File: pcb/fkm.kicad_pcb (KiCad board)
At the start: 2 copper layers, 50.3 x 33.5 mm, 12 parts, among them U2 18650, U3 AMS1117-3.3

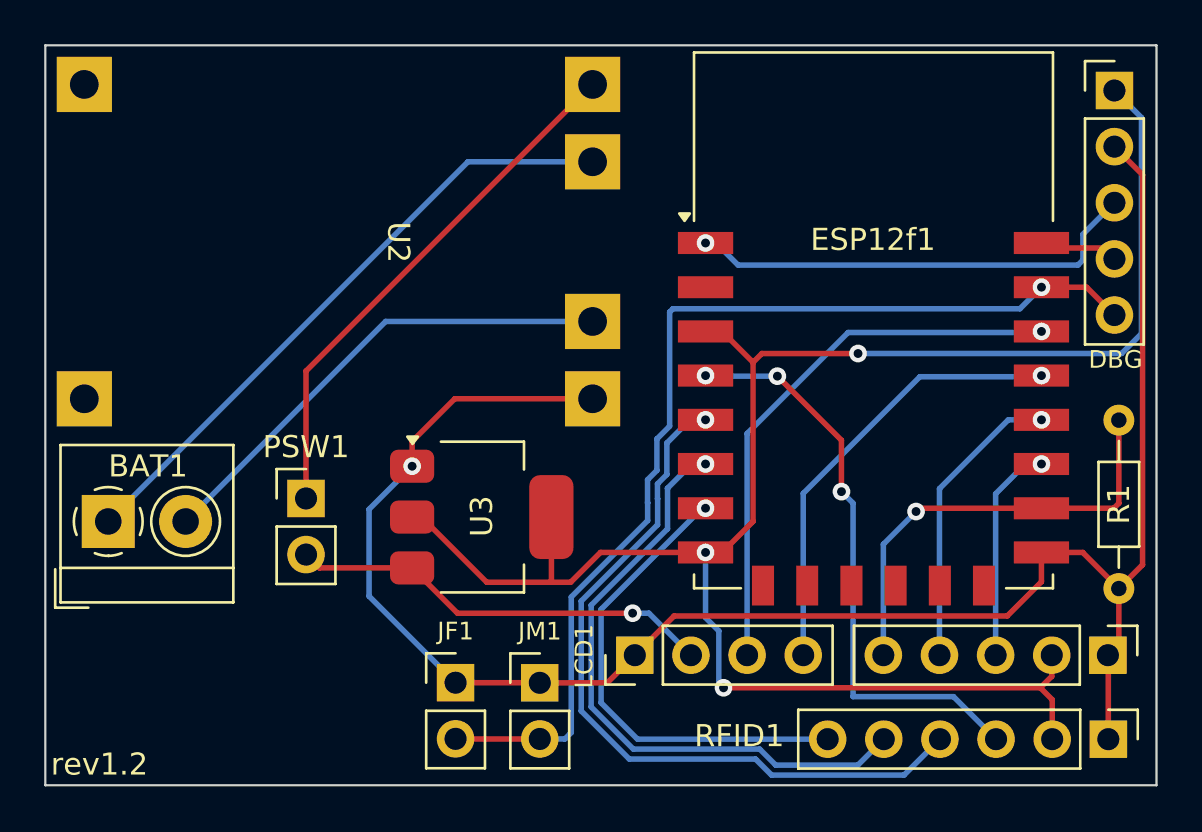
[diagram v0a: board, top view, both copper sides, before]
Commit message: wip(pcb): rev 2.0 pcb (esp32) - to re-do
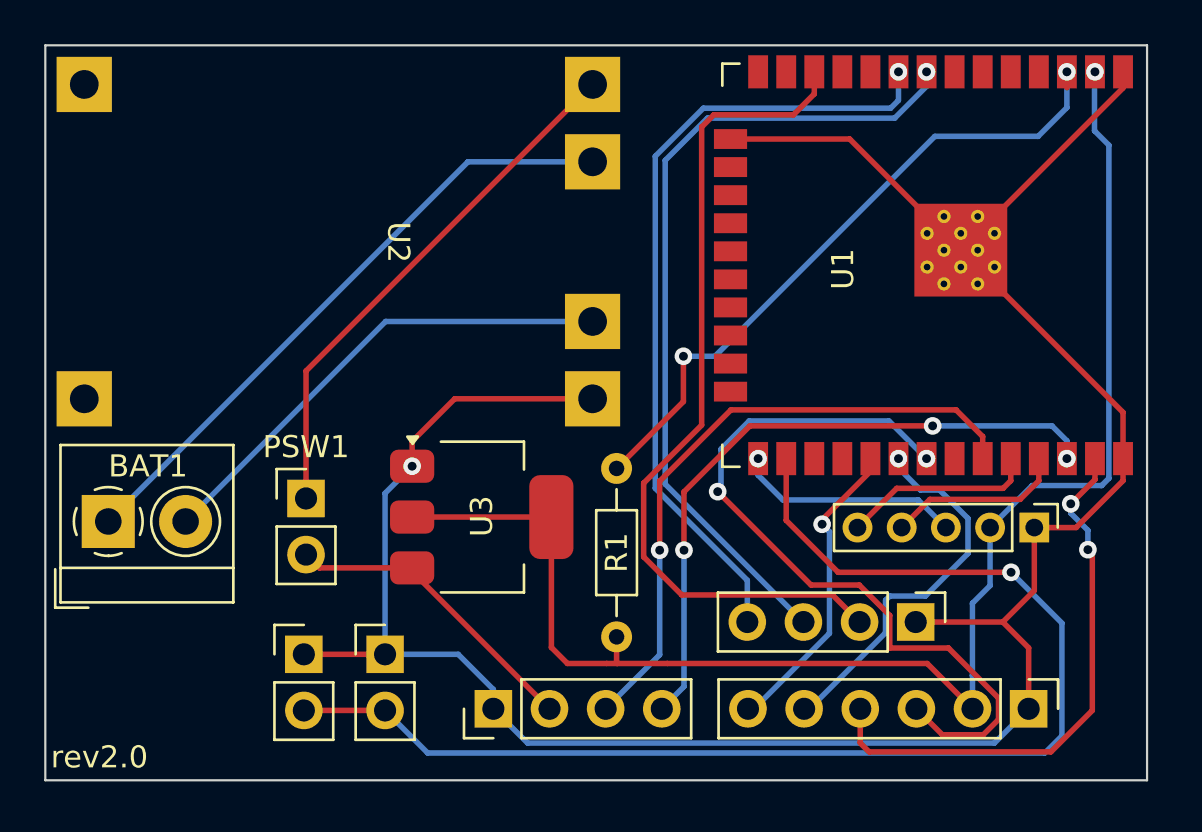
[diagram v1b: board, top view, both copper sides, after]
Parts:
- removed ESP12f1: ESP-12F/E, RF_Module:ESP-12E
- added U1: ESP32-WROOM-32, RF_Module:ESP32-WROOM-32, F.Cu at (107.2, 84.7)
- BTN1: value Conn_01x05 -> Conn_01x04; footprint Connector_PinHeader_2.54mm:PinHeader_1x05_P2.54mm_Vertical -> Connector_PinHeader_2.54mm:PinHeader_1x04_P2.54mm_Vertical
- DBG1: footprint Connector_PinHeader_2.54mm:PinHeader_1x05_P2.54mm_Vertical -> Connector_PinHeader_2.00mm:PinHeader_1x05_P2.00mm_Vertical
- moved R1 24.8 mm to (92.5, 101.5), turned to 90 degrees
- moved DBG1 20.1 mm to (111.4, 96.6), turned to -90 degrees
- moved BTN1 8.82 mm to (106.1, 100.9)
- moved JM1 7.12 mm to (82.0, 102.3)
- moved JF1 6.98 mm to (78.4, 102.3)
- moved LCD1 6.84 mm to (87.0, 104.8)
- moved RFID1 3.86 mm to (111.2, 104.8)
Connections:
- BTN1 pad 2: +3.3V -> Net-(BTN1-Pin_2)
- DBG1 pad 1: +3.3V -> GND
- DBG1 pad 2: GND -> +3.3V
- DBG1 pad 3: Net-(DBG1-Pin_3) -> BM
- DBG1 pad 4: Net-(DBG1-Pin_4) -> TX
- DBG1 pad 5: Net-(DBG1-Pin_5) -> RX
- JF1 pad 2: Net-(DBG1-Pin_5) -> JACK
- JM1 pad 2: Net-(DBG1-Pin_5) -> JACK
- LCD1 pad 3: Net-(ESP12f1-GPIO5) -> SDA
- LCD1 pad 4: Net-(ESP12f1-GPIO4) -> SCL
- R1 pad 1: Net-(BTN1-Pin_5) -> +3.3V
- R1 pad 2: GND -> Net-(U1-EN)
- RFID1 pad 3: Net-(ESP12f1-GPIO16) -> MISO
- RFID1 pad 4: Net-(ESP12f1-GPIO14) -> MOSI
- RFID1 pad 5: Net-(ESP12f1-GPIO12) -> SCK
- RFID1 pad 6: Net-(ESP12f1-GPIO13) -> CS
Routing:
- net JACK: track 0.00 -> 57.7 mm, vias 0 -> 1
- net Net-(DBG1-Pin_5): track 47.3 -> 0.00 mm, vias 1 -> 0
- net Net-(BTN1-Pin_2): track 0.00 -> 38.2 mm
- net MISO: track 0.00 -> 35.4 mm, vias 0 -> 2
- net Net-(ESP12f1-GPIO14): track 34.0 -> 0.00 mm, vias 1 -> 0
- net Net-(U1-EN): track 0.00 -> 30.7 mm, vias 0 -> 2
- net SCL: track 0.00 -> 29.9 mm, vias 0 -> 3
- net SDA: track 0.00 -> 28.8 mm, vias 0 -> 1
- net Net-(ESP12f1-GPIO12): track 28.3 -> 0.00 mm, vias 1 -> 0
- net Net-(BTN1-Pin_3): track 9.93 -> 37.4 mm
- net Net-(ESP12f1-GPIO16): track 26.4 -> 0.00 mm, vias 3 -> 0
- net Net-(ESP12f1-GPIO5): track 25.3 -> 0.00 mm, vias 1 -> 0
- net MOSI: track 0.00 -> 25.2 mm, vias 0 -> 2
- net Net-(BTN1-Pin_4): track 13.4 -> 36.1 mm
- net Net-(ESP12f1-GPIO13): track 21.8 -> 0.00 mm, vias 1 -> 0
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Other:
- board size 50.3 x 33.5 mm -> 49.8 x 33.3 mm
- board text added: "rev2.0"
- board text removed: "DBG"
- board text removed: "rev1.2"

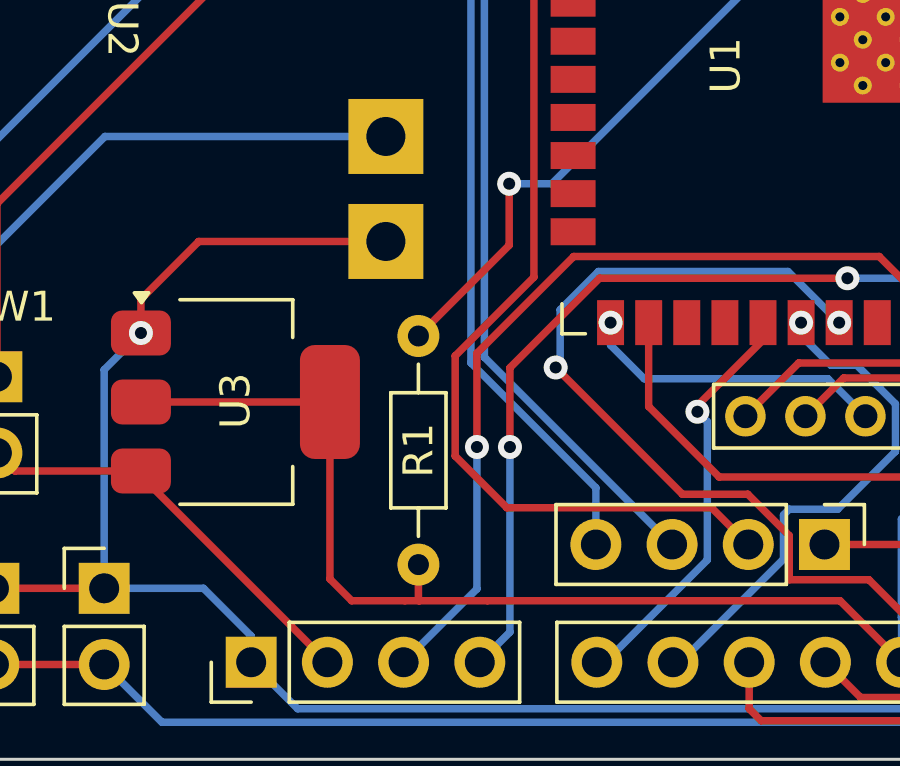
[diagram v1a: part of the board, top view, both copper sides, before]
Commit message: feat(pcb): battery level input (ADC)
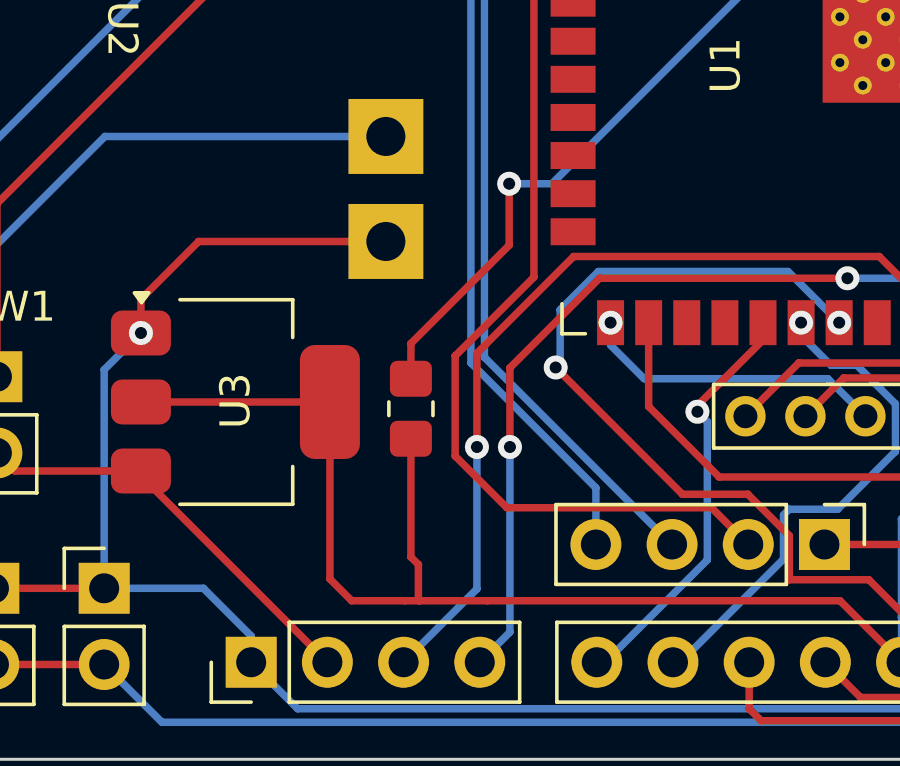
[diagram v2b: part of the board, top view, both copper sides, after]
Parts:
- R1: footprint Resistor_THT:R_Axial_DIN0204_L3.6mm_D1.6mm_P7.62mm_Horizontal -> Resistor_SMD:R_0805_2012Metric_Pad1.20x1.40mm_HandSolder
- moved R1 5.20 mm to (92.3, 96.3)
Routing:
- net +3.3V: track 67.1 -> 71.4 mm
- net Net-(U1-EN): track 30.7 -> 32.2 mm
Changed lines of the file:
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@@
 		)
 	)
-	(footprint "Resistor_THT:R_Axial_DIN0204_L3.6mm_D1.6mm_P7.62mm_Horizontal"
+	(footprint "Resistor_SMD:R_0805_2012Metric_Pad1.20x1.40mm_HandSolder"
 		(layer "F.Cu")
-		(at 92.525 101.545 90)
-		(descr "Resistor, Axial_DIN0204 series, Axial, Horizontal, pin pitch=7.62mm, 0.167W, length*diameter=3.6*1.6mm^2, http://cdn-reichelt.de/documents/datenblatt/B400/1_4W%23YAG.pdf")
-		(tags "Resistor Axial_DIN0204 series Axial Horizontal pin pitch 7.62mm 0.167W length 3.6mm diameter 1.6mm")
+		(at 92.275 96.35 90)
+		(descr "Resistor SMD 0805 (2012 Metric), square (rectangular) end terminal, IPC_7351 nominal with elongated pad for handsoldering. (Body size source: IPC-SM-782 page 72, https://www.pcb-3d.com/wordpress/wp-content/uploads/ipc-sm-782a_amendment_1_and_2.pdf), generated with kicad-footprint-generator")
+		(tags "resistor handsolder")
 		(property "Reference" "R1"
-			(at 3.81 0 -90)
+			(at 0 -1.65 90)
 			(layer "F.SilkS")
+			(hide yes)
 			(effects
 				(font
@@
 		)
 		(property "Value" "R10000"
-			(at 3.81 1.92 -90)
+			(at 0 1.65 90)
 			(layer "F.Fab")
 			(hide yes)
@@
 			)
 		)
-		(property "Footprint" "Resistor_THT:R_Axial_DIN0204_L3.6mm_D1.6mm_P7.62mm_Horizontal"
+		(property "Footprint" "Resistor_SMD:R_0805_2012Metric_Pad1.20x1.40mm_HandSolder"
 			(at 0 0 90)
 			(unlocked yes)
@@
 		(sheetname "Root")
 		(sheetfile "fkm.kicad_sch")
-		(attr through_hole)
-		(fp_line
-			(start 5.73 -0.92)
-			(end 1.89 -0.92)
-			(stroke
-				(width 0.12)
-				(type solid)
-			)
-			(layer "F.SilkS")
-		)
-		(fp_line
-			(start 1.89 -0.92)
-			(end 1.89 0.92)
-			(stroke
-				(width 0.12)
-				(type solid)
-			)
-			(layer "F.SilkS")
-		)
-		(fp_line
-			(start 6.68 0)
-			(end 5.73 0)
-			(stroke
-				(width 0.12)
-				(type solid)
-			)
-			(layer "F.SilkS")
-		)
-		(fp_line
-			(start 0.94 0)
-			(end 1.89 0)
-			(stroke
-				(width 0.12)
-				(type solid)
-			)
-			(layer "F.SilkS")
-		)
+		(attr smd)
 		(fp_line
-			(start 5.73 0.92)
-			(end 5.73 -0.92)
+			(start -0.227064 -0.735)
+			(end 0.227064 -0.735)
 			(stroke
 				(width 0.12)
@@
 		)
 		(fp_line
-			(start 1.89 0.92)
-			(end 5.73 0.92)
+			(start -0.227064 0.735)
+			(end 0.227064 0.735)
 			(stroke
 				(width 0.12)
@@
 		)
 		(fp_line
-			(start 8.57 -1.05)
-			(end -0.95 -1.05)
+			(start 1.85 -0.95)
+			(end 1.85 0.95)
 			(stroke
 				(width 0.05)
@@
 		)
 		(fp_line
-			(start -0.95 -1.05)
-			(end -0.95 1.05)
+			(start -1.85 -0.95)
+			(end 1.85 -0.95)
 			(stroke
 				(width 0.05)
@@
 		)
 		(fp_line
-			(start 8.57 1.05)
-			(end 8.57 -1.05)
+			(start 1.85 0.95)
+			(end -1.85 0.95)
 			(stroke
 				(width 0.05)
@@
 		)
 		(fp_line
-			(start -0.95 1.05)
-			(end 8.57 1.05)
+			(start -1.85 0.95)
+			(end -1.85 -0.95)
 			(stroke
 				(width 0.05)
@@
 		)
 		(fp_line
-			(start 5.61 -0.8)
-			(end 2.01 -0.8)
+			(start 1 -0.625)
+			(end 1 0.625)
 			(stroke
 				(width 0.1)
@@
 		)
 		(fp_line
-			(start 2.01 -0.8)
-			(end 2.01 0.8)
+			(start -1 -0.625)
+			(end 1 -0.625)
 			(stroke
 				(width 0.1)
@@
 		)
 		(fp_line
-			(start 7.62 0)
-			(end 5.61 0)
+			(start 1 0.625)
+			(end -1 0.625)
 			(stroke
 				(width 0.1)
@@
 		)
 		(fp_line
-			(start 0 0)
-			(end 2.01 0)
-			(stroke
-				(width 0.1)
-				(type solid)
-			)
-			(layer "F.Fab")
-		)
-		(fp_line
-			(start 5.61 0.8)
-			(end 5.61 -0.8)
-			(stroke
-				(width 0.1)
-				(type solid)
-			)
-			(layer "F.Fab")
-		)
-		(fp_line
-			(start 2.01 0.8)
-			(end 5.61 0.8)
+			(start -1 0.625)
+			(end -1 -0.625)
 			(stroke
 				(width 0.1)
@@
 		)
 		(fp_text user "${REFERENCE}"
-			(at 3.81 0 -90)
+			(at 0 0 90)
 			(layer "F.Fab")
 			(effects
 				(font
-					(size 0.72 0.72)
-					(thickness 0.108)
+					(size 0.5 0.5)
+					(thickness 0.08)
 				)
 			)
 		)
-		(pad "1" thru_hole circle
-			(at 0 0 90)
-			(size 1.4 1.4)
-			(drill 0.7)
-			(layers "*.Cu" "*.Mask")
-			(remove_unused_layers no)
+		(pad "1" smd roundrect
+			(at -1 0 90)
+			(size 1.2 1.4)
+			(layers "F.Cu" "F.Paste" "F.Mask")
+			(roundrect_rratio 0.208333)
 			(net 5 "+3.3V")
 			(pintype "passive")
 		)
-		(pad "2" thru_hole oval
-			(at 7.62 0 90)
-			(size 1.4 1.4)
-			(drill 0.7)
-			(layers "*.Cu" "*.Mask")
-			(remove_unused_layers no)
+		(pad "2" smd roundrect
+			(at 1 0 90)
+			(size 1.2 1.4)
+			(layers "F.Cu" "F.Paste" "F.Mask")
+			(roundrect_rratio 0.208333)
 			(net 3 "Net-(U1-EN)")
 			(pintype "passive")
 		)
-		(model "${KICAD8_3DMODEL_DIR}/Resistor_THT.3dshapes/R_Axial_DIN0204_L3.6mm_D1.6mm_P7.62mm_Horizontal.wrl"
+		(model "${KICAD8_3DMODEL_DIR}/Resistor_SMD.3dshapes/R_0805_2012Metric.wrl"
 			(offset
 				(xyz 0 0 0)
@@
 	)
 	(segment
-		(start 92.525 93.925)
+		(start 95.55 88.85)
 		(end 95.55 90.9)
 		(width 0.25)
@@
 	)
 	(segment
+		(start 92.275 94.175)
+		(end 92.275 95.35)
+		(width 0.25)
+		(layer "F.Cu")
+		(net 3)
+	)
+	(segment
 		(start 95.55 90.9)
-		(end 95.55 88.85)
+		(end 92.275 94.175)
 		(width 0.25)
 		(layer "F.Cu")
@@
 	)
 	(segment
+		(start 92.275 101.295)
+		(end 92.275 97.35)
+		(width 0.25)
+		(layer "F.Cu")
+		(net 5)
+	)
+	(segment
 		(start 89.575 102.025)
 		(end 90.3 102.75)
@@
 		(width 0.25)
 		(layer "F.Cu")
+		(net 5)
+	)
+	(segment
+		(start 92.525 101.545)
+		(end 92.275 101.295)
+		(width 0.25)
+		(layer "F.Cu")

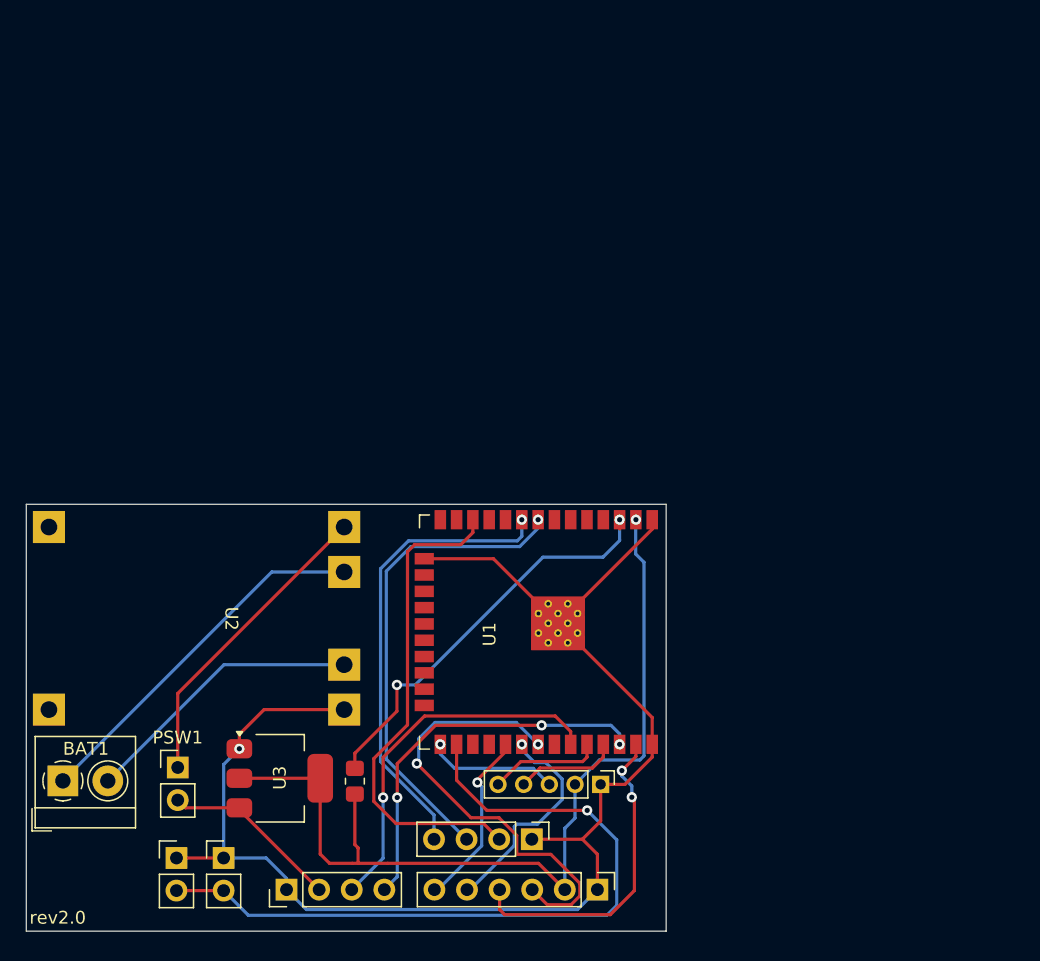
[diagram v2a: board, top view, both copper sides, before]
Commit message: wip(pcb): re-wire everything (now its not messy)
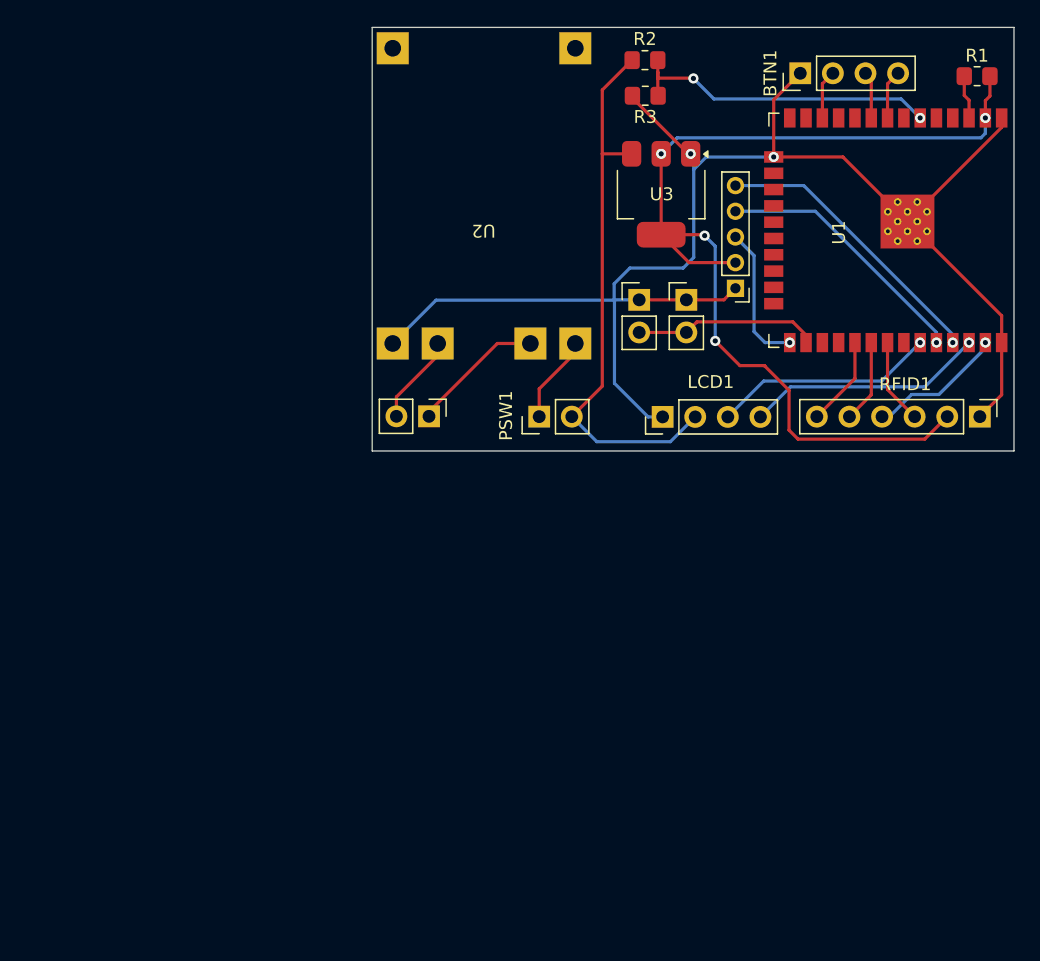
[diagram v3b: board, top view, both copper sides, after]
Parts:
- added R2: R10000, Resistor_SMD:R_0805_2012Metric_Pad1.20x1.40mm_HandSolder, F.Cu at (114.9, 40.2)
- added R3: R10000, Resistor_SMD:R_0805_2012Metric_Pad1.20x1.40mm_HandSolder, F.Cu at (114.9, 43.0)
- BAT1: value Screw_Terminal_01x02 -> BAT1; footprint TerminalBlock_4Ucon:TerminalBlock_4Ucon_1x02_P3.50mm_Horizontal -> Connector_PinHeader_2.54mm:PinHeader_1x02_P2.54mm_Vertical
- moved R1 73.3 mm to (140.8, 41.4), turned to 180 degrees
- moved BTN1 63.2 mm to (127.0, 41.2), turned to 90 degrees
- moved JF1 56.5 mm to (114.4, 58.9)
- moved JM1 56.5 mm to (118.1, 58.9)
- moved U3 54.3 mm to (116.1, 50.6), turned to -90 degrees
- moved RFID1 47.4 mm to (141.0, 68.0)
- moved LCD1 47.1 mm to (116.2, 68.0)
- moved U1 41.5 mm to (134.4, 53.4)
- moved BAT1 40.3 mm to (98.0, 67.9), turned to -90 degrees
- moved DBG1 40.1 mm to (121.9, 58.0), turned to 180 degrees
- moved PSW1 39.2 mm to (106.6, 68.0), turned to 90 degrees
- moved U2 36.7 mm to (102.3, 53.0), turned to 180 degrees
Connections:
- net Net-(BTN1-Pin_2) renamed BTN3
- BTN1 pad 3: Net-(BTN1-Pin_3) -> BTN1
- BTN1 pad 4: Net-(BTN1-Pin_4) -> BTN2
- DBG1 pad 4: TX -> RX
- DBG1 pad 5: RX -> TX
- U1 pad 6: unconnected-(U1-IO34-Pad6) -> BAT_ADC
- U1 pad 8: Net-(BTN1-Pin_3) -> BTN2
- U1 pad 9: Net-(BTN1-Pin_4) -> BTN1
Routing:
- net JACK: track 57.7 -> 14.4 mm, vias 1 -> 0
- net Net-(BTN1-Pin_3): track 37.4 -> 0.00 mm, vias 1 -> 0
- net Net-(BTN1-Pin_4): track 36.1 -> 0.00 mm, vias 1 -> 0
- net BTN3: track 38.2 -> 3.82 mm
- net +5V: track 14.0 -> 43.2 mm
- net Net-(U1-EN): track 32.2 -> 3.11 mm, vias 2 -> 0
- net MISO: track 35.4 -> 6.64 mm, vias 2 -> 0
- net BAT_ADC: track 0.00 -> 25.5 mm, vias 0 -> 2
- net Net-(BAT1-Pin_1): track 28.7 -> 10.5 mm
- net Net-(PSW1-Pin_1): track 24.1 -> 6.87 mm
- net Net-(BAT1-Pin_2): track 22.2 -> 7.01 mm
- net MOSI: track 25.2 -> 10.7 mm, vias 2 -> 1
- net TX: track 8.08 -> 22.4 mm, vias 0 -> 1
- net RX: track 8.81 -> 20.4 mm, vias 0 -> 1
- net SDA: track 28.8 -> 17.4 mm
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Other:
- board size 49.8 x 33.3 mm -> 50 x 33 mm

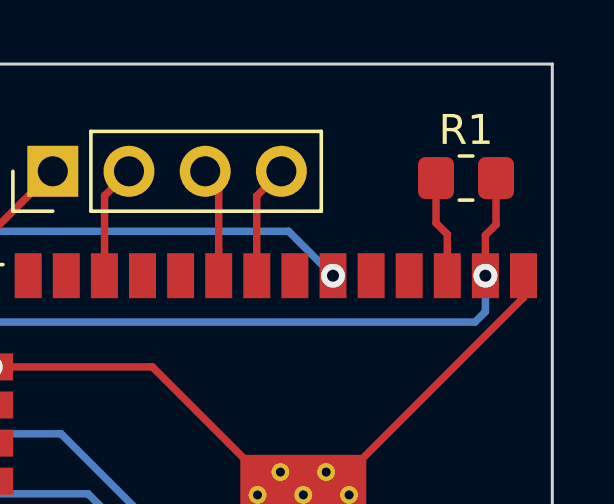
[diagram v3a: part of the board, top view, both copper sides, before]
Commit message: feat(pcb): decoupling capacitor
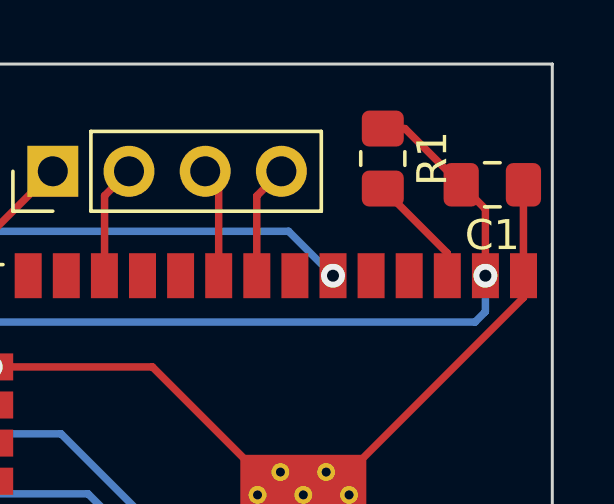
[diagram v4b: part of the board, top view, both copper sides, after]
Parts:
- added C1: C, Capacitor_SMD:C_0805_2012Metric_Pad1.18x1.45mm_HandSolder, F.Cu at (141.6, 41.6)
- moved R1 2.85 mm to (138.0, 40.8), turned to -90 degrees
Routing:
- net +3.3V: track 79.2 -> 82.8 mm
- net GND: track 112.9 -> 116.0 mm
- net Net-(U1-EN): track 3.11 -> 3.80 mm
